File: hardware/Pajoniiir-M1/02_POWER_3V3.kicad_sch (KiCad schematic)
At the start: 14 parts, among them U8 TPS62132RGTR

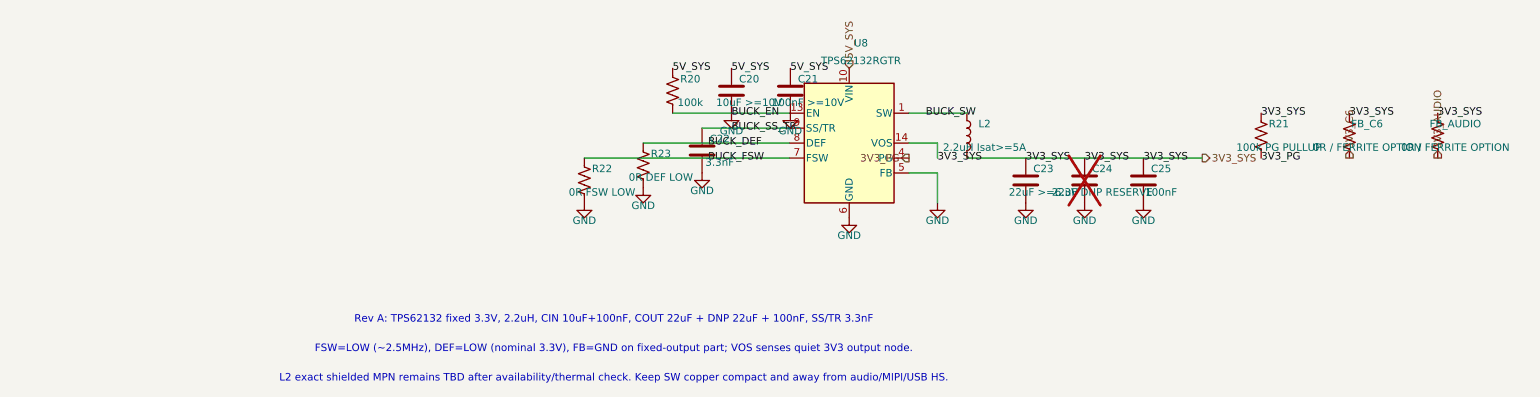
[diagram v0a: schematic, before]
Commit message: hardware: snap child sheets 01-05 to 25 mil grid
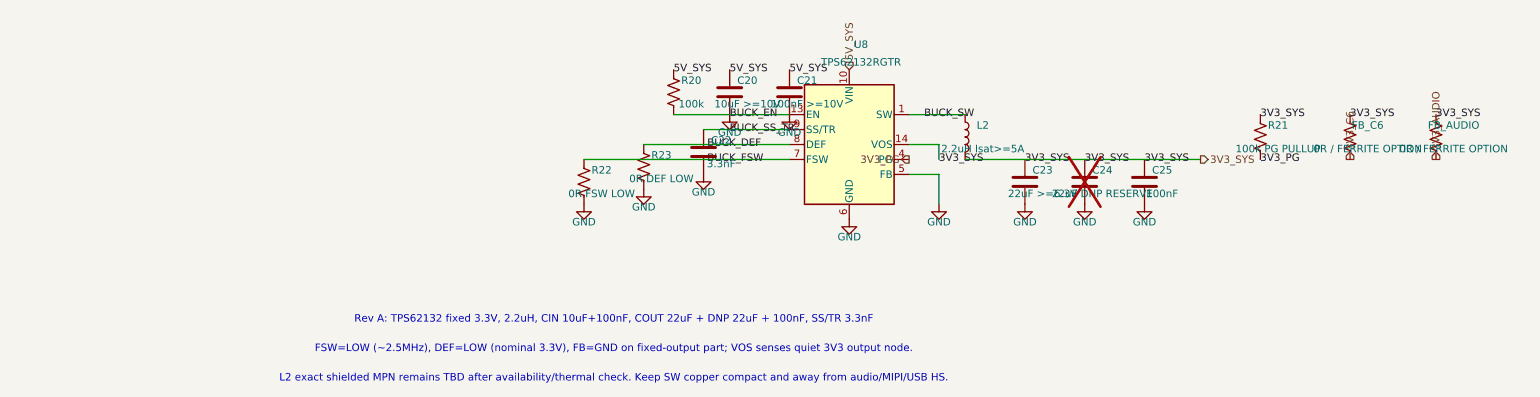
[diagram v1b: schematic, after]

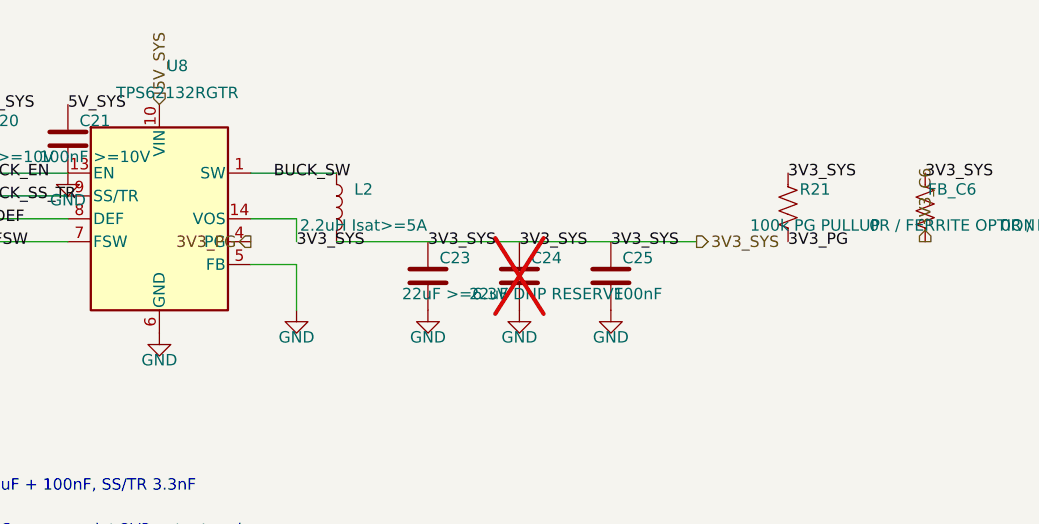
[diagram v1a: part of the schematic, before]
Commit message: hardware: bind core hierarchical ports to nets
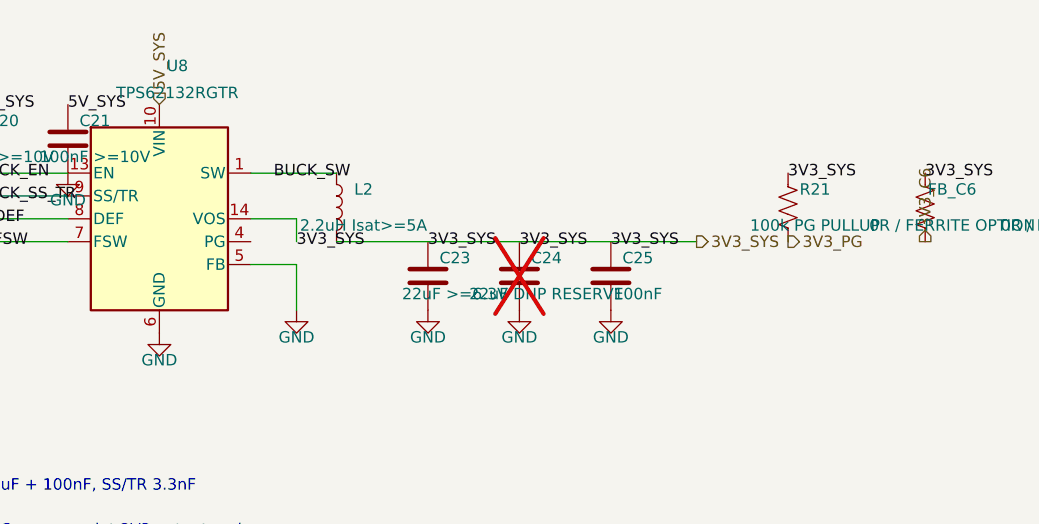
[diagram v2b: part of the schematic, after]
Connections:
- net 3V3_PG: no longer U8.4 (PG)
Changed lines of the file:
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@@
     (instances (project "Pajoniiir-M1" (path "/2c8dd352-b7b8-4d9e-8f93-5dd43be2a100/31000002-6b2a-4a3a-8c91-000000000002" (reference "#PWR0210") (unit 1))))
   )
-  (hierarchical_label "3V3_PG" (shape output) (at 130.175 57.785 180) (effects (font (size 1.27 1.27))))
+  (hierarchical_label "3V3_PG" (shape output) (at 189.865 57.785 0) (effects (font (size 1.27 1.27))))
   (symbol
     (lib_id "Device:R_US") (at 189.865 53.975 0) (unit 1)
@@
   )
   (label "3V3_SYS" (at 189.865 50.165 0) (effects (font (size 1.27 1.27))))
-  (label "3V3_PG" (at 189.865 57.785 0) (effects (font (size 1.27 1.27))))
   (symbol
     (lib_id "Device:R_US") (at 205.105 53.975 0) (unit 1)

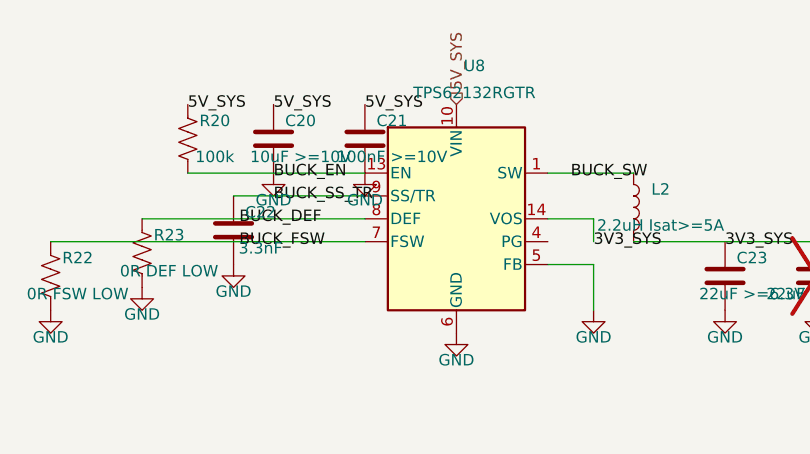
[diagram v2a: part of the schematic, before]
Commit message: hardware: fix 3V3 buck enable and power-good nets
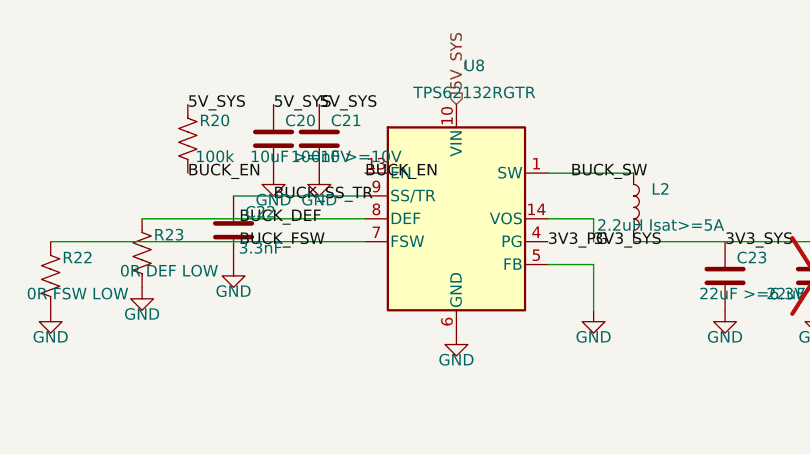
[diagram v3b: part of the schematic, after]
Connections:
- net 3V3_PG: now also U8.4 (PG)
- net GND: no longer R20.2, U8.13 (EN)
- new net BUCK_EN: R20.2, U8.13 (EN)
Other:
- moved on the sheet: C21
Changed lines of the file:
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@@
   )
   (symbol
-    (lib_id "Device:C") (at 109.855 46.355 0) (unit 1)
-    (exclude_from_sim no) (in_bom yes) (on_board yes) (dnp no)
-    (property "Reference" "C21" (at 112.855 44.355 0) (effects (font (size 1.27 1.27))))
-    (property "Value" "100nF >=10V" (at 112.855 48.355 0) (effects (font (size 1.27 1.27))))
-    (property "Footprint" "Capacitor_SMD:C_0603_1608Metric" (at 109.855 46.355 0) (effects (font (size 1.27 1.27)) (hide yes)))
-    (property "Datasheet" "~" (at 109.855 46.355 0) (effects (font (size 1.27 1.27)) (hide yes)))
+    (lib_id "Device:C") (at 104.775 46.355 0) (unit 1)
+    (exclude_from_sim no) (in_bom yes) (on_board yes) (dnp no)
+    (property "Reference" "C21" (at 107.775 44.355 0) (effects (font (size 1.27 1.27))))
+    (property "Value" "100nF >=10V" (at 107.775 48.355 0) (effects (font (size 1.27 1.27))))
+    (property "Footprint" "Capacitor_SMD:C_0603_1608Metric" (at 104.775 46.355 0) (effects (font (size 1.27 1.27)) (hide yes)))
+    (property "Datasheet" "~" (at 104.775 46.355 0) (effects (font (size 1.27 1.27)) (hide yes)))
     (pin "1") (pin "2")
     (instances (project "Pajoniiir-M1" (path "/2c8dd352-b7b8-4d9e-8f93-5dd43be2a100/31000002-6b2a-4a3a-8c91-000000000002" (reference "C21") (unit 1))))
   )
-  (label "5V_SYS" (at 109.855 42.545 0) (effects (font (size 1.27 1.27))))
-  (symbol
-    (lib_id "power:GND") (at 109.855 50.165 0) (unit 1)
-    (exclude_from_sim no) (in_bom yes) (on_board yes) (dnp no)
-    (property "Reference" "#PWR0202" (at 109.855 56.165 0) (effects (font (size 1.27 1.27)) (hide yes)))
-    (property "Value" "GND" (at 109.855 53.165 0) (effects (font (size 1.27 1.27))))
-    (property "Footprint" "" (at 109.855 50.165 0) (effects (font (size 1.27 1.27)) (hide yes)))
-    (property "Datasheet" "" (at 109.855 50.165 0) (effects (font (size 1.27 1.27)) (hide yes)))
+  (label "5V_SYS" (at 104.775 42.545 0) (effects (font (size 1.27 1.27))))
+  (symbol
+    (lib_id "power:GND") (at 104.775 50.165 0) (unit 1)
+    (exclude_from_sim no) (in_bom yes) (on_board yes) (dnp no)
+    (property "Reference" "#PWR0202" (at 104.775 56.165 0) (effects (font (size 1.27 1.27)) (hide yes)))
+    (property "Value" "GND" (at 104.775 53.165 0) (effects (font (size 1.27 1.27))))
+    (property "Footprint" "" (at 104.775 50.165 0) (effects (font (size 1.27 1.27)) (hide yes)))
+    (property "Datasheet" "" (at 104.775 50.165 0) (effects (font (size 1.27 1.27)) (hide yes)))
     (pin "1")
     (instances (project "Pajoniiir-M1" (path "/2c8dd352-b7b8-4d9e-8f93-5dd43be2a100/31000002-6b2a-4a3a-8c91-000000000002" (reference "#PWR0202") (unit 1))))
@@
   )
   (label "5V_SYS" (at 90.17 42.545 0) (effects (font (size 1.27 1.27))))
-  (wire (pts (xy 90.17 50.165) (xy 109.855 50.165)) (stroke (width 0) (type default)))
-  (label "BUCK_EN" (at 99.695 50.165 0) (effects (font (size 1.27 1.27))))
+  (label "BUCK_EN" (at 90.17 50.165 0) (effects (font (size 1.27 1.27))))
+  (label "BUCK_EN" (at 109.855 50.165 0) (effects (font (size 1.27 1.27))))
   (symbol
     (lib_id "Device:C") (at 95.25 56.515 0) (unit 1)
@@
     (instances (project "Pajoniiir-M1" (path "/2c8dd352-b7b8-4d9e-8f93-5dd43be2a100/31000002-6b2a-4a3a-8c91-000000000002" (reference "#PWR0210") (unit 1))))
   )
+  (label "3V3_PG" (at 130.175 57.785 0) (effects (font (size 1.27 1.27))))
   (hierarchical_label "3V3_PG" (shape output) (at 189.865 57.785 0) (effects (font (size 1.27 1.27))))
   (symbol

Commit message: hardware: declare verified rail power sources for ERC
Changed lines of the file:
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@@
   (text "FSW=LOW (~2.5MHz), DEF=LOW (nominal 3.3V), FB=GND on fixed-output part; VOS senses quiet 3V3 output node." (exclude_from_sim no) (at 80 90 0) (effects (font (size 1.27 1.27))))
   (text "L2 exact shielded MPN remains TBD after availability/thermal check. Keep SW copper compact and away from audio/MIPI/USB HS." (exclude_from_sim no) (at 80 95 0) (effects (font (size 1.27 1.27))))
+  (symbol
+    (lib_id "power:PWR_FLAG")
+    (at 120.015 42.545 0)
+    (unit 1)
+    (exclude_from_sim no)
+    (in_bom yes)
+    (on_board yes)
+    (dnp no)
+    (property "Reference" "#FLG0201" (at 120.015 44.45 0) (effects (font (size 1.27 1.27)) (hide yes)))
+    (property "Value" "PWR_FLAG" (at 120.015 46.355000000000004 0) (effects (font (size 1.27 1.27))))
+    (property "Footprint" "" (at 120.015 42.545 0) (effects (font (size 1.27 1.27)) (hide yes)))
+    (property "Datasheet" "~" (at 120.015 42.545 0) (effects (font (size 1.27 1.27)) (hide yes)))
+    (property "Description" "Special symbol for telling ERC where power comes from" (at 120.015 42.545 0) (effects (font (size 1.27 1.27)) (hide yes)))
+    (pin "1")
+    (instances (project "Pajoniiir-M1" (path "/2c8dd352-b7b8-4d9e-8f93-5dd43be2a100/31000002-6b2a-4a3a-8c91-000000000002" (reference "#FLG0201") (unit 1))))
+  )
   (sheet_instances (path "/" (page "3")))
   (embedded_fonts no)

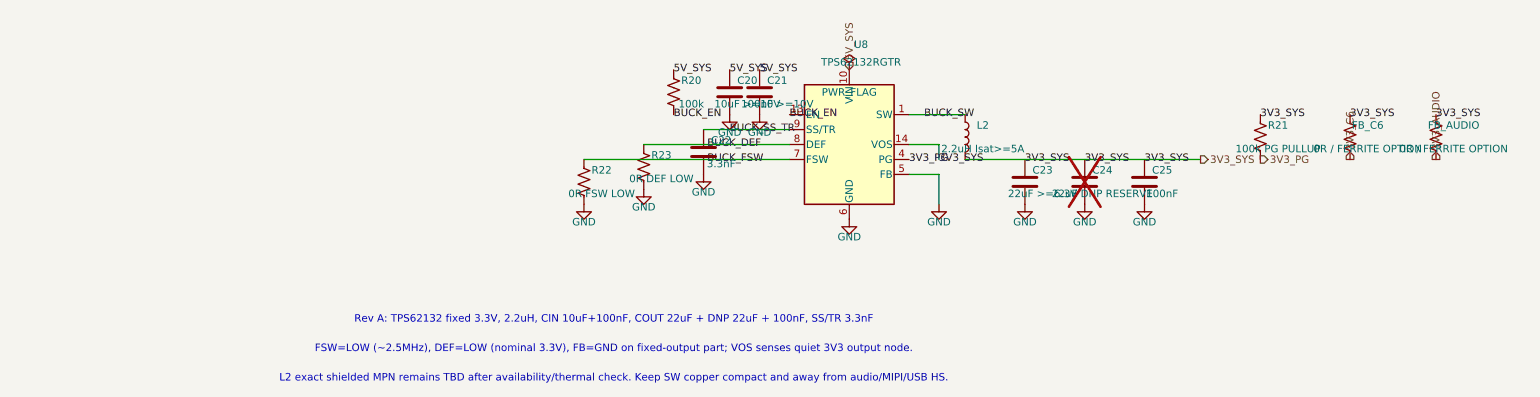
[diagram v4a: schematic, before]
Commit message: hardware: lock 2.2uH power inductors to XGL4030-222MEC
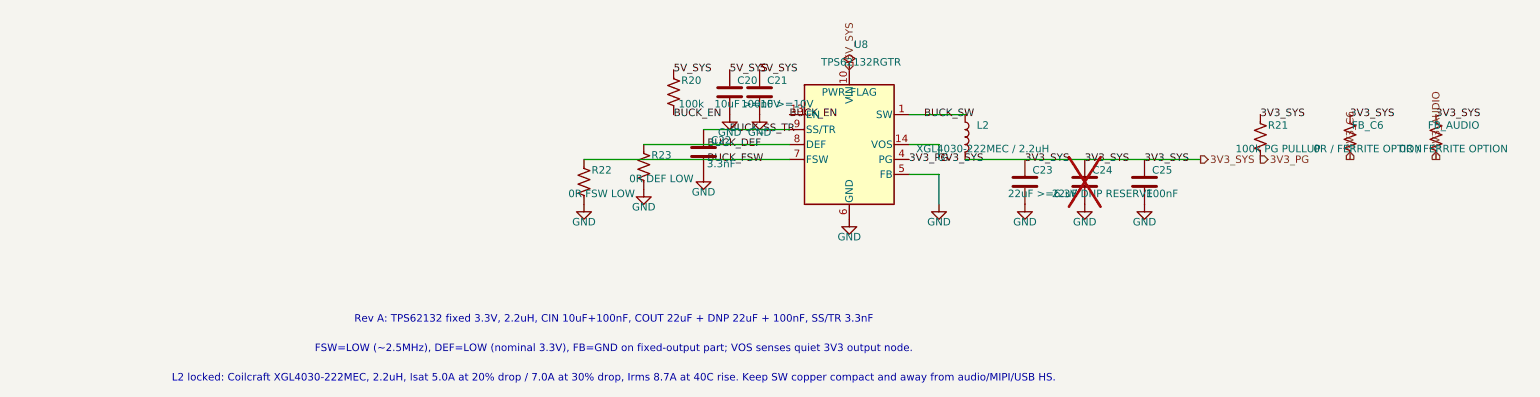
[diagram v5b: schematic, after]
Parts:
- L2: value 2.2uH Isat>=5A -> XGL4030-222MEC / 2.2uH; footprint Inductor_SMD:L_4.0x4.0mm_TBD -> Inductor_SMD:L_Coilcraft_XxL4030
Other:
- note added: "L2 locked: Coilcraft XGL4030-222MEC, 2.2uH, Isat 5.0A at 20% drop / 7.0A at 30% drop, Irms 8.7A at 40C rise. Keep SW copper compact and away from audio/MIPI/USB HS."
- note removed: "L2 exact shielded MPN remains TBD after availability/thermal check. Keep SW copper compact and away from audio/MIPI/USB HS."
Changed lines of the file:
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@@
     (exclude_from_sim no) (in_bom yes) (on_board yes) (dnp no)
     (property "Reference" "L2" (at 142.7 51.975 0) (effects (font (size 1.27 1.27))))
-    (property "Value" "2.2uH Isat>=5A" (at 142.7 55.975 0) (effects (font (size 1.27 1.27))))
-    (property "Footprint" "Inductor_SMD:L_4.0x4.0mm_TBD" (at 139.7 53.975 0) (effects (font (size 1.27 1.27)) (hide yes)))
-    (property "Datasheet" "~" (at 139.7 53.975 0) (effects (font (size 1.27 1.27)) (hide yes)))
+    (property "Value" "XGL4030-222MEC / 2.2uH" (at 142.7 55.975 0) (effects (font (size 1.27 1.27))))
+    (property "Footprint" "Inductor_SMD:L_Coilcraft_XxL4030" (at 139.7 53.975 0) (effects (font (size 1.27 1.27)) (hide yes)))
+    (property "Datasheet" "https://www.coilcraft.com/en-us/products/power/shielded-inductors/molded-inductor/xgl/xgl4030/xgl4030-222/" (at 139.7 53.975 0) (effects (font (size 1.27 1.27)) (hide yes)))
     (pin "1") (pin "2")
     (instances (project "Pajoniiir-M1" (path "/2c8dd352-b7b8-4d9e-8f93-5dd43be2a100/31000002-6b2a-4a3a-8c91-000000000002" (reference "L2") (unit 1))))
@@
   (text "Rev A: TPS62132 fixed 3.3V, 2.2uH, CIN 10uF+100nF, COUT 22uF + DNP 22uF + 100nF, SS/TR 3.3nF" (exclude_from_sim no) (at 80 85 0) (effects (font (size 1.27 1.27))))
   (text "FSW=LOW (~2.5MHz), DEF=LOW (nominal 3.3V), FB=GND on fixed-output part; VOS senses quiet 3V3 output node." (exclude_from_sim no) (at 80 90 0) (effects (font (size 1.27 1.27))))
-  (text "L2 exact shielded MPN remains TBD after availability/thermal check. Keep SW copper compact and away from audio/MIPI/USB HS." (exclude_from_sim no) (at 80 95 0) (effects (font (size 1.27 1.27))))
+  (text "L2 locked: Coilcraft XGL4030-222MEC, 2.2uH, Isat 5.0A at 20% drop / 7.0A at 30% drop, Irms 8.7A at 40C rise. Keep SW copper compact and away from audio/MIPI/USB HS." (exclude_from_sim no) (at 80 95 0) (effects (font (size 1.27 1.27))))
   (symbol
     (lib_id "power:PWR_FLAG")

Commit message: hardware: pin Rev-A symbols to local library copies
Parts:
- U8: symbol Regulator_Switching:TPS62132 -> Pajoniiir-M1:TPS62132_M1
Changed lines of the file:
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@@
   )
   (symbol
-    (lib_id "Regulator_Switching:TPS62132")
+    (lib_id "Pajoniiir-M1:TPS62132_M1")
     (at 120.015 55.245 0) (unit 1)
     (exclude_from_sim no) (in_bom yes) (on_board yes) (dnp no)
